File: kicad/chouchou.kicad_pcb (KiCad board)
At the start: 2 copper layers, 210.5 x 114.4 mm, 51 parts

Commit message: updated PDB (without images)
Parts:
- removed ?: LOGO, images:butterfly_right
- removed ?: LOGO, images:butterfly_left
- removed RP2040Zero1: , RP2040-Zero
- removed S21, S22, S23, S24, S25, S26, S27, S28, S29, S30, S31, S32, S33, S34, S35, S36, S37, S38, S39, S40: , PG1350
- removed _1, _2, _3, _4, _5, _6, _7, _8: , MountingHole_2.2mm_M2_Pad_Via
- added D1: , ceoloide:diode_tht_sod123, B.Cu at (40.9, 139.8)
- added D10: , ceoloide:diode_tht_sod123, B.Cu at (111.0, 200.8)
- added D11: , ceoloide:diode_tht_sod123, B.Cu at (229.2, 137.2)
- added D12: , ceoloide:diode_tht_sod123, B.Cu at (224.8, 120.8)
- added D13: , ceoloide:diode_tht_sod123, B.Cu at (204.9, 134.5)
- added D14: , ceoloide:diode_tht_sod123, B.Cu at (197.7, 119.1)
- added D15: , ceoloide:diode_tht_sod123, B.Cu at (183.7, 138.4)
- added D16: , ceoloide:diode_tht_sod123, B.Cu at (175.2, 123.7)
- added D17: , ceoloide:diode_tht_sod123, B.Cu at (167.7, 156.4)
- added D18: , ceoloide:diode_tht_sod123, B.Cu at (157.9, 142.4)
- added D19: , ceoloide:diode_tht_sod123, B.Cu at (170.0, 199.8)
- added D2: , ceoloide:diode_tht_sod123, B.Cu at (45.3, 123.4)
- added D20: , ceoloide:diode_tht_sod123, B.Cu at (154.7, 209.3)
- added D3: , ceoloide:diode_tht_sod123, B.Cu at (64.6, 138.8)
- added D4: , ceoloide:diode_tht_sod123, B.Cu at (71.8, 123.3)
- added D5: , ceoloide:diode_tht_sod123, B.Cu at (85.4, 143.4)
- added D6: , ceoloide:diode_tht_sod123, B.Cu at (93.9, 128.7)
- added D7: , ceoloide:diode_tht_sod123, B.Cu at (100.9, 162.1)
- added D8: , ceoloide:diode_tht_sod123, B.Cu at (110.7, 148.2)
- added D9: , ceoloide:diode_tht_sod123, B.Cu at (95.8, 191.3)
- added DISP1: , ceoloide:display_nice_view, F.Cu at (130.2, 159.7)
- added H1: , ceoloide:mounting_hole_plated, F.Cu at (55.3, 111.1)
- added H2: , ceoloide:mounting_hole_plated, F.Cu at (205.1, 111.1)
- added H3: , ceoloide:mounting_hole_plated, F.Cu at (75.8, 150.0)
- added H4: , ceoloide:mounting_hole_plated, F.Cu at (184.6, 150.0)
- added H5: , ceoloide:mounting_hole_plated, F.Cu at (104.4, 129.2)
- added H6: , ceoloide:mounting_hole_plated, F.Cu at (156.0, 129.2)
- added H7: , ceoloide:mounting_hole_plated, F.Cu at (92.7, 209.4)
- added H8: , ceoloide:mounting_hole_plated, F.Cu at (167.7, 209.4)
- added JST1: , ceoloide:battery_connector_jst_ph_2, B.Cu at (130.2, 165.2)
- added LOGO1: , ceoloide:utility_ergogen_logo, B.Cu at (152.2, 173.7)
- added REF**: XIAO-nRF52840-Plus-SMD-Cutout, XIAO-nRF52840-Plus-SMD-Cutout, B.Cu at (130.2, 152.2)
- added RST1: , ceoloide:reset_switch_tht_top, F.Cu at (130.2, 183.7)
- S1, S10, S11, S12, S13, S14, S15, S16, S17, S18, S19, S2, S20, S3, S4, S5, S6, S7, S8, S9: footprint PG1350 -> ceoloide:switch_choc_v1_v2; moved to B.Cu
- moved S18 143.7 mm to (106.7, 204.0), turned to 58 degrees
- moved S17 138.7 mm to (91.4, 194.5), turned to 58 degrees
- moved S9 111.3 mm to (223.8, 136.6), turned to 15 degrees
- moved S16 94.1 mm to (152.7, 143.7), turned to 35 degrees
- moved S10 92.9 mm to (219.4, 120.2), turned to 15 degrees
- moved S15 92.8 mm to (162.5, 157.6), turned to 35 degrees
- moved S14 84.0 mm to (169.9, 124.4), turned to 30 degrees
- moved S13 82.7 mm to (178.4, 139.2), turned to 30 degrees
- moved S12 81.7 mm to (192.3, 119.4), turned to 25 degrees
- moved S11 79.3 mm to (199.5, 134.8), turned to 25 degrees
- moved S1 69.9 mm to (36.6, 136.6)
- moved S4 69.9 mm to (68.1, 119.4)
- moved S5 69.9 mm to (82.0, 139.2)
- moved S8 69.9 mm to (107.7, 143.7)
- moved S19 69.9 mm to (169.0, 194.5)
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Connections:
- S1 pad : (no net) -> pinky_bottom
- S1 pad 1: GP12 -> D11
- S1 pad 2: GND -> pinky_bottom
- S10 pad : (no net) -> mirror_pinky_top
- S10 pad 1: GP10 -> D11
- S10 pad 2: GND -> mirror_pinky_top
- S11 pad : (no net) -> mirror_ring_bottom
- S11 pad 1: GP7 -> D12
- S11 pad 2: GND -> mirror_ring_bottom
- S12 pad : (no net) -> mirror_ring_top
- S12 pad 1: GP3 -> D12
- S12 pad 2: GND -> mirror_ring_top
- S13 pad : (no net) -> mirror_middle_bottom
- S13 pad 1: GP6 -> D13
- S13 pad 2: GND -> mirror_middle_bottom
- S14 pad : (no net) -> mirror_middle_top
- S14 pad 1: GP2 -> D13
- S14 pad 2: GND -> mirror_middle_top
- S15 pad : (no net) -> mirror_index_bottom
- S15 pad 1: GP5 -> D14
- S15 pad 2: GND -> mirror_index_bottom
- S16 pad : (no net) -> mirror_index_top
- S16 pad 1: GP1 -> D14
- S16 pad 2: GND -> mirror_index_top
- S17 pad : (no net) -> inner_cluster
- S17 pad 1: GP4 -> D11
- S17 pad 2: GND -> inner_cluster
- S18 pad : (no net) -> outer_cluster
- S18 pad 1: GP0 -> D12
- S18 pad 2: GND -> outer_cluster
- S19 pad : (no net) -> mirror_inner_cluster
- S19 pad 1: GP8 -> D13
- S19 pad 2: GND -> mirror_inner_cluster
- S2 pad : (no net) -> pinky_top
- S2 pad 1: GP26 -> D11
- S2 pad 2: GND -> pinky_top
- S20 pad : (no net) -> mirror_outer_cluster
- S20 pad 1: GP9 -> D14
- S20 pad 2: GND -> mirror_outer_cluster
- S3 pad : (no net) -> ring_bottom
- S3 pad 1: GP13 -> D12
- S3 pad 2: GND -> ring_bottom
- S4 pad : (no net) -> ring_top
- S4 pad 1: GP27 -> D12
- S4 pad 2: GND -> ring_top
- S5 pad : (no net) -> middle_bottom
- S5 pad 1: GP14 -> D13
- S5 pad 2: GND -> middle_bottom
- S6 pad : (no net) -> middle_top
- S6 pad 1: GP28 -> D13
- S6 pad 2: GND -> middle_top
- S7 pad : (no net) -> index_bottom
- S7 pad 1: GP15 -> D14
- S7 pad 2: GND -> index_bottom
- S8 pad : (no net) -> index_top
- S8 pad 1: GP29 -> D14
- S8 pad 2: GND -> index_top
- S9 pad : (no net) -> mirror_pinky_bottom
- S9 pad 1: GP11 -> D11
- S9 pad 2: GND -> mirror_pinky_bottom
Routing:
- net GND: track 819.8 -> 27.7 mm, vias 0 -> 2
- net D11: track 0.00 -> 367.1 mm, vias 0 -> 8
- net D12: track 0.00 -> 288.3 mm, vias 0 -> 7
- net D13: track 0.00 -> 244.1 mm, vias 0 -> 5
- net D14: track 0.00 -> 180.9 mm, vias 0 -> 6
- net GP12: track 129.0 -> 0.00 mm
- net D6: track 0.00 -> 127.6 mm
- net D1: track 0.00 -> 122.5 mm, vias 0 -> 2
- net GP26: track 120.5 -> 0.00 mm
- net D0: track 0.00 -> 109.9 mm, vias 0 -> 2
- net D3: track 0.00 -> 108.3 mm
- net GP7: track 105.8 -> 0.00 mm
- net D2: track 0.00 -> 102.8 mm
- net GP3: track 100.8 -> 0.00 mm
- net GP13: track 97.2 -> 0.00 mm
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- added copper zone on B.Cu, net GND
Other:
- board text added: "ChouChou Flight --------------------- Original Design github.com/dlip (Dane Lipscombe) --------------------- Flight Edition Modifications github.com/lozengedrop (Zach Logan)"
- board text added: "Powered By Ergogen"

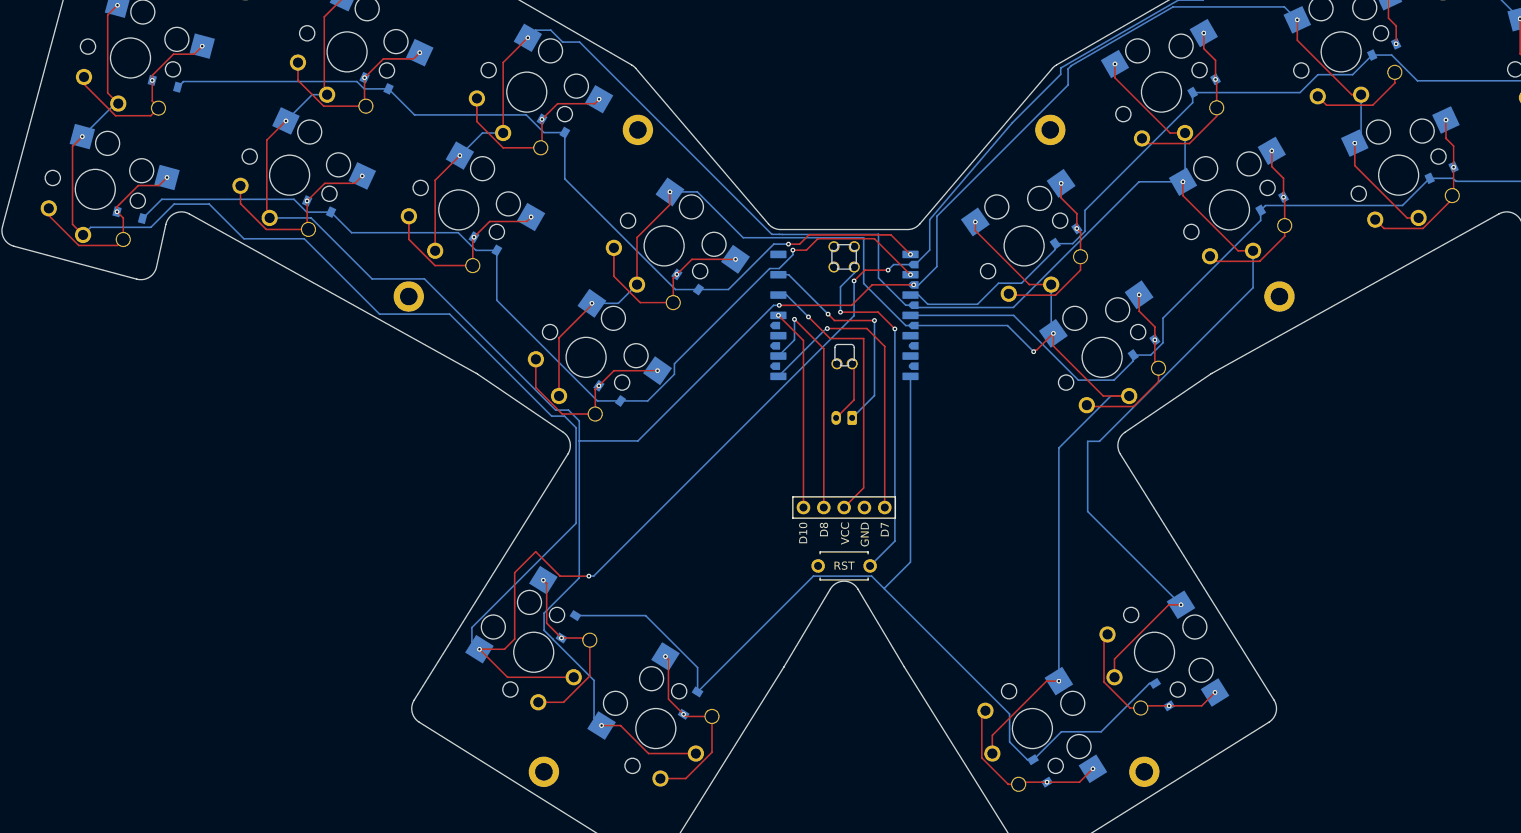
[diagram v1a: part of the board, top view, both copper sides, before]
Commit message: Add graphics to the pcb
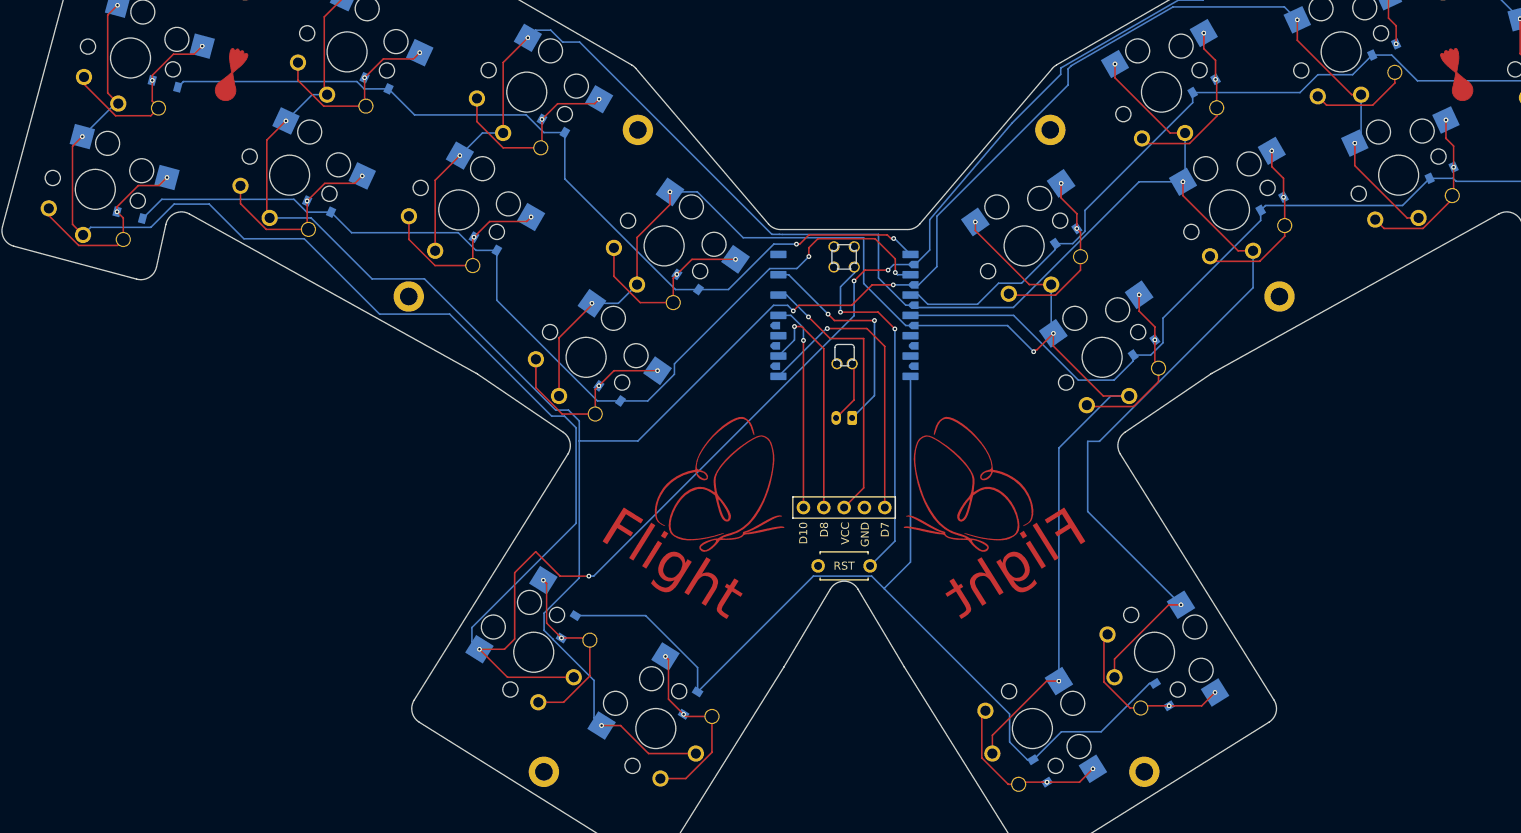
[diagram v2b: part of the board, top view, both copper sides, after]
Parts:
- added G***: LOGO, Library:butterfly_flight_right_FCu, F.Cu at (144.9, 174.5)
- added G***: LOGO, Library:butterfly_flight_left_FCu, F.Cu at (115.5, 174.5)
- added REF**: LozengeDrop, Library:LozengeDrop, F.Cu at (206.7, 122.0)
- added REF**: LozengeDrop, Library:LozengeDrop, F.Cu at (53.7, 122.0)
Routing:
- net D12: track 288.3 -> 286.7 mm
- net D1: track 122.5 -> 123.8 mm
- net D8: track 30.5 -> 29.2 mm
- net mirror_inner_cluster: track 22.2 -> 21.1 mm
- net mirror_outer_cluster: track 22.1 -> 21.1 mm
- net pinky_top: track 24.4 -> 23.4 mm
- net D10: track 25.3 -> 26.2 mm
- net pinky_bottom: track 24.2 -> 23.3 mm
- net mirror_middle_top: track 22.1 -> 21.2 mm
- net mirror_middle_bottom: track 22.2 -> 21.4 mm
- net mirror_index_bottom: track 22.2 -> 21.3 mm
- net D13: track 244.1 -> 243.3 mm
- net mirror_ring_bottom: track 22.0 -> 21.3 mm
- net inner_cluster: track 24.1 -> 23.5 mm
- net D11: track 367.1 -> 366.5 mm
